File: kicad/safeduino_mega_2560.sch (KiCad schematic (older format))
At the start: 97 parts, among them X1 USBB-1J

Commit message: Продолжил переделывать SafeDuino MEGA 2560.
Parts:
- removed XP16, XP26, XP27, XP28, XP32, XP36, XP37, XP39, XP40, XP48, XP53, XP62, XP65, XP67, XP68, XP7: ~, IWconnectors:1_pin, symbol LFconnectors:PIN_M_1
- added LL1: MMZ2012R601AT000, IWsmd_case:SMD0805, symbol LFtransformator:INDUCTOR
- added XP7, XP8: PLS-2, IWconnectors:PIN_ARRAY_2x1, symbol LFconnectors:connector_2pin_gost
- added XS11: PBS-10, IWconnectors:PIN_ARRAY_10x1, symbol LFconnectors:connector_10pin_gost
- C13, C14, C15, C16, C17, C18, C19, C2, C20, C22, C23, C3, C4, C8, R10, R11, R12, R13, R14, R17, R18, R19, R2, R3, R4, R5, R6, R7, R8, R9: footprint IWsmd_case:SMD0805 -> IWsmd_case:SMD0603
- C6: value 100мк 10В -> 4.7 мк 50В
- DA1: value P10LU-0505ELF -> SPU03L-05
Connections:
- net labels added: USB_D+, USB_D-
- net labels removed: UD+, UD-
- wire segments 524 -> 523
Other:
- note added: "R19 необходим для создания импульса команды\nRESET на ATMEGA 2560 через конденсатор С2"
- note removed: "PB"
- note removed: "PD"
- note removed: "PE"
- note removed: "PH"
- note removed: "R19 необходим для подачи команды RESET на ATMEGA 2560 через\nконденсатор С2"
- moved on the sheet: C1, C6, DA1, FU1, VD8

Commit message: Продолжил переделывать печатную плату SafeDuino MEGA 2560.
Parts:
- XS10: value 2214SM-36G-75-PCP -> PBD-28; footprint IWconnectors:PIN_ARRAY_18x2 -> IWconnectors:PIN_ARRAY_14x2; symbol LFconnectors:connector_36pin_gost -> LFconnectors:connector_28pin_gost
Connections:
- wire segments 523 -> 515
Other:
- note removed: "PA0"
- note removed: "PA1"
- note removed: "PA2"
- note removed: "PA3"
- note removed: "PA4"
- note removed: "PA5"
- note removed: "PA6"
- note removed: "PA7"
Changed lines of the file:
@@
 Text Notes 19000 5050 0    60   ~ 0
 SCK
-Text Notes 19000 8150 0    60   ~ 0
-GND
 Text Notes 19000 6750 0    60   ~ 0
 PC2
 Text Notes 19000 6850 0    60   ~ 0
 PC3
-Text Notes 19000 7350 0    60   ~ 0
-PA7
-Text Notes 19000 7450 0    60   ~ 0
-PA6
-Text Notes 19000 7550 0    60   ~ 0
-PA5
-Text Notes 19000 7650 0    60   ~ 0
-PA4
-Text Notes 19000 7750 0    60   ~ 0
-PA3
-Text Notes 19000 7850 0    60   ~ 0
-PA2
-Text Notes 19000 7950 0    60   ~ 0
-PA1
-Text Notes 19000 8050 0    60   ~ 0
-PA0
-Text Notes 19000 8250 0    60   ~ 0
-GND
 Text Notes 19000 7250 0    60   ~ 0
 PC7
@@
 Text Notes 19000 7050 0    60   ~ 0
 PC5
-Connection ~ 18500 8200
+Connection ~ 18500 7400
 Text Label 18050 4700 0    60   ~ 0
 MPU_VCC
 Wire Wire Line
-	18500 8100 18500 8200
-Wire Wire Line
-	18600 8100 18500 8100
-Text Label 18050 8200 0    60   ~ 0
+	18500 7300 18500 7400
+Wire Wire Line
+	18600 7300 18500 7300
+Text Label 18050 7400 0    60   ~ 0
 GND
 Wire Wire Line
 	18600 4900 18050 4900
-Text Label 18050 4900 0    60   ~ 0
-PB0
 Wire Wire Line
 	18600 5000 18050 5000
-Text Label 18050 5000 0    60   ~ 0
-PB1
 Wire Wire Line
 	18600 5100 18050 5100
-Text Label 18050 5100 0    60   ~ 0
-PB2
 Wire Wire Line
 	18600 5200 18050 5200
-Text Label 18050 5200 0    60   ~ 0
-PB3
 Wire Wire Line
 	18600 5300 18050 5300
@@
 Text Label 18050 7200 0    60   ~ 0
 PC7
-Text Label 18050 7300 0    60   ~ 0
-PA7
-Text Label 18050 7400 0    60   ~ 0
-PA6
-Text Label 18050 7500 0    60   ~ 0
-PA5
-Text Label 18050 7600 0    60   ~ 0
-PA4
-Text Label 18050 7700 0    60   ~ 0
-PA3
-Text Label 18050 7800 0    60   ~ 0
-PA2
-Text Label 18050 7900 0    60   ~ 0
-PA1
-Text Label 18050 8000 0    60   ~ 0
-PA0
-Wire Wire Line
-	18600 8200 18500 8200
-$Comp
-L LFconnectors:connector_36pin_gost XS10
-U 1 1 64EB12AA
-P 18600 4700
-F 0 "XS10" H 18850 5050 71  0000 L CNN
-F 1 "2214SM-36G-75-PCP" H 18350 4950 71  0000 L CNN
-F 2 "IWconnectors:PIN_ARRAY_18x2" H 18950 4850 50  0001 C CNN
-F 3 "" H 18600 4700 60  0000 C CNN
-	1    18600 4700
-	1    0    0    -1
-$EndComp
+Wire Wire Line
+	18600 7400 18500 7400
 $Comp
 L LFtransformator:INDUCTOR LL1
@@
 	18050 7200 18600 7200
 Wire Wire Line
-	18050 7300 18600 7300
-Wire Wire Line
-	18050 7400 18600 7400
-Wire Wire Line
-	18050 7500 18600 7500
-Wire Wire Line
-	18050 7600 18600 7600
-Wire Wire Line
-	18050 7700 18600 7700
-Wire Wire Line
 	18050 6000 18600 6000
 Wire Wire Line
-	18050 7800 18600 7800
-Wire Wire Line
-	18050 7900 18600 7900
-Wire Wire Line
-	18050 8000 18600 8000
-Wire Wire Line
-	18050 8200 18500 8200
+	18050 7400 18500 7400
 Wire Wire Line
 	18050 6100 18600 6100
@@
 Text Notes 20400 9100 0    60   ~ 0
 GND
+Text Label 10350 3000 0    50   ~ 0
+PB0
+Text Label 10350 3100 0    50   ~ 0
+PB1
+Text Label 10350 3200 0    50   ~ 0
+PB2
+Text Label 10350 3300 0    50   ~ 0
+PB3
+Text Label 18050 5100 0    60   ~ 0
+MOSI
+Text Label 18050 5200 0    60   ~ 0
+MISO
+Text Label 18050 5000 0    60   ~ 0
+SCK
+Text Label 18050 4900 0    60   ~ 0
+SS
+Text Notes 19000 7350 0    60   ~ 0
+GND
+Text Notes 19000 7450 0    60   ~ 0
+GND
+$Comp
+L LFconnectors:connector_28pin_gost XS10
+U 1 1 64EB12AA
+P 18600 4700
+F 0 "XS10" H 18850 5050 71  0000 L CNN
+F 1 "PBD-28" H 18750 4950 71  0000 L CNN
+F 2 "IWconnectors:PIN_ARRAY_14x2" H 18950 4850 50  0001 C CNN
+F 3 "" H 18600 4700 60  0000 C CNN
+	1    18600 4700
+	1    0    0    -1
+$EndComp
 $EndSCHEMATC

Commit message: Закончил предварительную трассировку платы SafeDuino MEGA 2560.
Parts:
- XS11: value PBS-10 -> PBS-8; footprint IWconnectors:PIN_ARRAY_10x1 -> IWconnectors:PIN_ARRAY_8x1; symbol LFconnectors:connector_10pin_gost -> LFconnectors:connector_8pin_gost
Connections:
- wire segments 515 -> 513
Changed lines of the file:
@@
 Wire Wire Line
 	4800 8100 5250 8100
-Text Label 19600 8350 0    60   ~ 0
-SS
+Text Label 19600 8550 0    60   ~ 0
+PD4
+Text Label 19600 8650 0    60   ~ 0
+PD5
 Text Label 19600 8750 0    60   ~ 0
-PD4
+PD6
+Text Label 19600 8950 0    60   ~ 0
+PE7
+Text Label 19600 9050 0    60   ~ 0
+PE6
+Text Label 19600 9150 0    60   ~ 0
+PE2
+Text Label 19600 8450 0    60   ~ 0
+PH7
 Text Label 19600 8850 0    60   ~ 0
-PD5
-Text Label 19600 8950 0    60   ~ 0
-PD6
-Text Label 19600 8650 0    60   ~ 0
-PE7
-Text Label 19600 8550 0    60   ~ 0
-PE6
-Text Label 19600 8450 0    60   ~ 0
-PE2
-Text Label 19600 9150 0    60   ~ 0
-PH7
-Text Label 19600 9050 0    60   ~ 0
 PH2
-Wire Wire Line
-	19600 8350 20000 8350
 Wire Wire Line
 	19600 8750 20000 8750
@@
 Text Notes 18750 11500 0    60   ~ 0
 VCC
-$Comp
-L LFconnectors:connector_10pin_gost XS11
-U 1 1 643A5231
-P 20000 8350
-F 0 "XS11" H 20150 8700 71  0000 L CNN
-F 1 "PBS-10" H 20150 8600 71  0000 L CNN
-F 2 "IWconnectors:PIN_ARRAY_10x1" H 20350 8500 50  0001 C CNN
-F 3 "" H 20000 8350 60  0000 C CNN
-	1    20000 8350
-	1    0    0    -1
-$EndComp
-Text Label 19600 9250 0    60   ~ 0
-GND
-Wire Wire Line
-	19600 9250 20000 9250
 Text Notes 20400 9200 0    60   ~ 0
 GND
-Text Notes 20400 9300 0    60   ~ 0
-GND
 Wire Wire Line
 	18050 5900 18600 5900
@@
 Wire Wire Line
 	18050 6700 18600 6700
-Text Notes 20400 8400 0    60   ~ 0
-GND
 Text Notes 20400 8500 0    60   ~ 0
 GND
@@
 	1    0    0    -1
 $EndComp
+$Comp
+L LFconnectors:connector_8pin_gost XS11
+U 1 1 643A5231
+P 20000 8450
+F 0 "XS11" H 20150 8800 71  0000 L CNN
+F 1 "PBS-8" H 20150 8700 71  0000 L CNN
+F 2 "IWconnectors:PIN_ARRAY_8x1" H 20350 8600 50  0001 C CNN
+F 3 "" H 20000 8450 60  0000 C CNN
+	1    20000 8450
+	1    0    0    -1
+$EndComp

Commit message: Оптимизировал трассировку печатной платы.
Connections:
- net labels removed: PB0, PB1, PB2, PB3
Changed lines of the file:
@@
 L LFcomponents:QUARTZ_RESONATOR Z2
 U 1 1 5256C28E
-P 10500 8350
-F 0 "Z2" H 10650 8700 71  0000 C CNN
-F 1 "16МГц" H 10650 8600 71  0000 C CNN
-F 2 "IWcomponents:HC-49SM" H 10500 8350 60  0001 C CNN
-F 3 "" H 10500 8350 60  0001 C CNN
-	1    10500 8350
-	1    0    0    -1
+P 10800 8350
+F 0 "Z2" H 10950 8700 71  0000 C CNN
+F 1 "16МГц" H 10950 8600 71  0000 C CNN
+F 2 "IWcomponents:HC-49SM" H 10800 8350 60  0001 C CNN
+F 3 "" H 10800 8350 60  0001 C CNN
+	1    10800 8350
+	-1   0    0    -1
 $EndComp
 Text Label 10650 9050 1    60   ~ 0
@@
 Text Notes 20400 9100 0    60   ~ 0
 GND
-Text Label 10350 3000 0    50   ~ 0
-PB0
-Text Label 10350 3100 0    50   ~ 0
-PB1
-Text Label 10350 3200 0    50   ~ 0
-PB2
-Text Label 10350 3300 0    50   ~ 0
-PB3
 Text Label 18050 5100 0    60   ~ 0
 MOSI

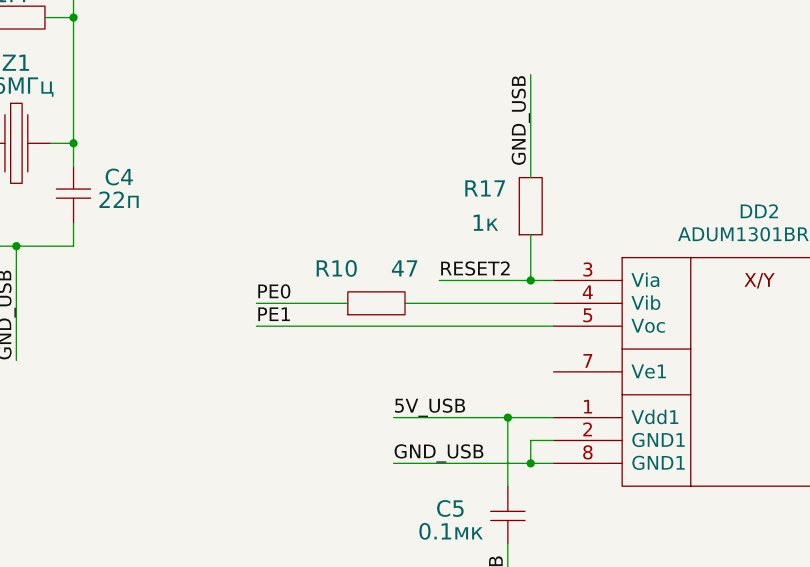
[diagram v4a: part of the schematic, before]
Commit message: Продолжил оптимизацию трассировки печатной платы.
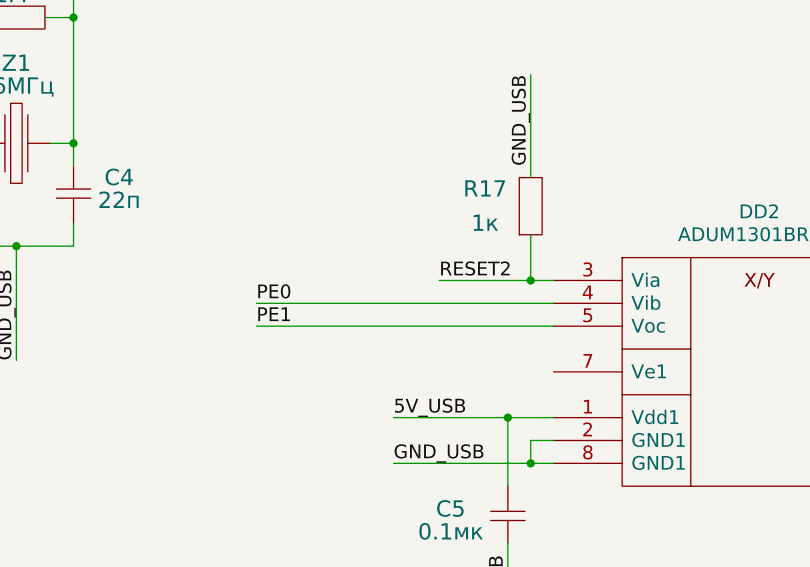
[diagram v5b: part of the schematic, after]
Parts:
- removed R10: 47, IWsmd_case:SMD0603, symbol LFresistor:RESISTOR
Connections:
- wire segments 513 -> 512
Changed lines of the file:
@@
 	7100 12800 7100 12900
 Wire Wire Line
-	6300 12200 5900 12200
-Wire Wire Line
 	5900 12300 7200 12300
-Wire Wire Line
-	7200 12200 6550 12200
 Wire Wire Line
 	20950 6400 21400 6400
@@
 Text Label 10500 12200 2    60   ~ 0
 RXD0
-$Comp
-L LFresistor:RESISTOR R10
-U 1 1 5260ED22
-P 6300 12200
-F 0 "R10" H 6250 12050 71  0000 C CNN
-F 1 "47" H 6550 12050 71  0000 C CNN
-F 2 "IWsmd_case:SMD0603" H 6300 12200 60  0001 C CNN
-F 3 "" H 6300 12200 60  0001 C CNN
-	1    6300 12200
-	1    0    0    1
-$EndComp
 Text Label 5900 12300 0    60   ~ 0
 PE1
@@
 	1    0    0    -1
 $EndComp
+Wire Wire Line
+	5900 12200 7200 12200
 $EndSCHEMATC

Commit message: Поправил схему для лучшей защиты от ЭМП и продолжил переделывать трассировку печатной платы.
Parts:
- removed C13, C14: 22п, IWsmd_case:SMD0603, symbol LFcapitors:CAPITORS
- removed R13, R7: 1M, IWsmd_case:SMD0603, symbol LFresistor:RESISTOR
- removed Z2: 16МГц, IWcomponents:HC-49SM, symbol LFcomponents:QUARTZ_RESONATOR
- added C24: 22мк 10В, IWsmd_case:CASE_B, symbol LFcapitors:CAPITORS_ELECTROLYTIC
- added C25: 0.1мк, IWsmd_case:SMD0603, symbol LFcapitors:CAPITORS
- added LL2: MMZ2012R601AT000, IWsmd_case:SMD0805, symbol LFtransformator:INDUCTOR
- added LL3: MMZ2012R600A, IWsmd_case:SMD0805, symbol LFtransformator:INDUCTOR
- added LL4: LQM21FN100N00L, IWsmd_case:SMD0805, symbol LFtransformator:INDUCTOR
- added Z2: CSTCE16M0V53-R0, IWsmd_case:CSTNE_G_8-13_99MHz, symbol LFcomponents:QUARTZ_CSTNE_G_CSTNE_V
- C1, C11, C12, C5, C9: footprint IWsmd_case:SMD0805 -> IWsmd_case:SMD0603
- C6: value 4.7 мк 50В -> 10 мк 25В
- C7: value 47мк 10В -> 22мк 10В
- LL1: value MMZ2012R601AT000 -> MMZ2012R600A
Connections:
- net labels added: RD+, RD-
- net labels removed: D+, D-
- wire segments 512 -> 507
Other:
- note added: "3.3V"
- note added: "ADC0"
- note added: "ADC1"
- note added: "ADC10"
- note added: "ADC11"
- note added: "ADC12"
- note added: "ADC13"
- note added: "ADC14"
- note added: "ADC15"
- note added: "ADC2"
- note added: "ADC3"
- note added: "ADC4"
- note added: "ADC5"
- note added: "ADC6"
- note added: "ADC7"
- note added: "ADC8"
- note added: "ADC9"
- note added: "PD4"
- note added: "PD5"
- note added: "PD6"
- note added: "PE2"
- note added: "PE6"
- note added: "PH2"
- note added: "PH7"
- note added: "VIN"
- moved on the sheet: C20, C21, C3, C4, C6, C7, DA1, DA3, R2, R3, VD1, VD2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

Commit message: Продолжил оптимизировать трассировку печатной платы.
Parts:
- removed C3, C4: 22п, IWsmd_case:SMD0603, symbol LFcapitors:CAPITORS
- removed R18: 1M, IWsmd_case:SMD0603, symbol LFresistor:RESISTOR
- removed VD7: PESD5V0L1BA,115, IWcomponents:SOD323, symbol LFdiod:STABILITRON_TWO
- removed Z1: 16МГц, IWcomponents:HC-49SM, symbol LFcomponents:QUARTZ_RESONATOR
- added Z1: CSTCE16M0V53-R0, IWsmd_case:CSTNE_G_8-13_99MHz, symbol LFcomponents:QUARTZ_CSTNE_G_CSTNE_V
- C24: value 22мк 10В -> 47мк 10В; footprint IWsmd_case:CASE_B -> IWsmd_case:CASE_C
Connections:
- wire segments 507 -> 492
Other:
- moved on the sheet: C1, C22, C23, R2, R3, R4, R6, VD3, VD4, VD8, Z3

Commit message: Продолжил оптимизировать трассировку печатной платы.
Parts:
- removed C12: 0.1мк, IWsmd_case:SMD0603, symbol LFcapitors:CAPITORS
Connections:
- wire segments 492 -> 488
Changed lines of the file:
@@
 	9650 10450 9650 10350
-Wire Wire Line
-	9200 10150 10650 10150
-Wire Wire Line
-	10650 10450 10650 10150
-Wire Wire Line
-	10650 10800 10650 10700
 Wire Wire Line
 	10150 10700 10150 10800
@@
 	9650 10700 9650 10800
 Connection ~ 10150 10250
-Connection ~ 10650 10150
 Connection ~ 9650 10350
 Wire Wire Line
@@
 Text Label 4600 12600 1    60   ~ 0
 GND_USB
-Text Label 11050 10150 2    60   ~ 0
+Text Label 10550 10150 2    60   ~ 0
 5V_USB
 Text Label 10550 10250 2    60   ~ 0
@@
 Text Label 10150 11300 1    60   ~ 0
 GND_USB
-$Comp
-L LFcapitors:CAPITORS C12
-U 1 1 52569AE0
-P 10650 10700
-F 0 "C12" V 10850 10450 71  0000 C CNN
-F 1 "0.1мк" V 10750 10450 71  0000 C CNN
-F 2 "IWsmd_case:SMD0603" H 10650 10700 60  0001 C CNN
-F 3 "" H 10650 10700 60  0001 C CNN
-	1    10650 10700
-	0    -1   -1   0
-$EndComp
 $Comp
 L LFcapitors:CAPITORS C11
@@
 	10150 10800 10150 11300
 Wire Wire Line
-	10150 10800 10650 10800
-Wire Wire Line
 	4700 5850 5250 5850
 Wire Wire Line
@@
 Wire Wire Line
 	10150 10250 10550 10250
-Wire Wire Line
-	10650 10150 11050 10150
 Wire Wire Line
 	9650 10350 10050 10350
@@
 	19600 9050 20000 9050
 Wire Wire Line
-	18500 4700 18600 4700
-Connection ~ 18500 4700
-Wire Wire Line
-	18500 4800 18500 4700
-Wire Wire Line
-	18600 4800 18500 4800
-Wire Wire Line
-	18050 4700 18500 4700
-Text Notes 19000 6150 0    60   ~ 0
+	18450 7400 18550 7400
+Connection ~ 18450 7400
+Wire Wire Line
+	18450 7300 18450 7400
+Wire Wire Line
+	18550 7300 18450 7300
+Wire Wire Line
+	18000 7400 18450 7400
+Text Notes 18950 6050 0    60   ~ 0
 PG0
-Text Notes 19000 6350 0    60   ~ 0
+Text Notes 18950 5850 0    60   ~ 0
 PG2
-Text Notes 19000 4750 0    60   ~ 0
-+5V
-Text Notes 19000 4850 0    60   ~ 0
-+5V
-Text Notes 19000 5350 0    60   ~ 0
+Text Notes 18950 7450 0    60   ~ 0
+GND
+Text Notes 18950 7350 0    60   ~ 0
+GND
+Text Notes 18950 6850 0    60   ~ 0
 PL0
-Text Notes 19000 5450 0    60   ~ 0
+Text Notes 18950 6750 0    60   ~ 0
 PL1
-Text Notes 19000 5550 0    60   ~ 0
+Text Notes 18950 6650 0    60   ~ 0
 PL2
-Text Notes 19000 5650 0    60   ~ 0
+Text Notes 18950 6550 0    60   ~ 0
 PL3
-Text Notes 19000 5750 0    60   ~ 0
+Text Notes 18950 6450 0    60   ~ 0
 PL4
-Text Notes 19000 5850 0    60   ~ 0
+Text Notes 18950 6350 0    60   ~ 0
 PL5
-Text Notes 19000 5950 0    60   ~ 0
+Text Notes 18950 6250 0    60   ~ 0
 PL6
-Text Notes 19000 6050 0    60   ~ 0
+Text Notes 18950 6150 0    60   ~ 0
 PL7
-Text Notes 19000 6250 0    60   ~ 0
+Text Notes 18950 5950 0    60   ~ 0
 PG1
-Text Notes 19000 6450 0    60   ~ 0
+Text Notes 18950 5750 0    60   ~ 0
 PD7
-Text Notes 19000 6550 0    60   ~ 0
+Text Notes 18950 5650 0    60   ~ 0
 PC0
-Text Notes 19000 6650 0    60   ~ 0
+Text Notes 18950 5550 0    60   ~ 0
 PC1
-Text Notes 19000 5250 0    60   ~ 0
+Text Notes 18950 6950 0    60   ~ 0
 MISO
-Text Notes 19000 5150 0    60   ~ 0
+Text Notes 18950 7050 0    60   ~ 0
 MOSI
-Text Notes 19000 4950 0    60   ~ 0
+Text Notes 18950 7250 0    60   ~ 0
 SS
-Text Notes 19000 5050 0    60   ~ 0
+Text Notes 18950 7150 0    60   ~ 0
 SCK
-Text Notes 19000 6750 0    60   ~ 0
+Text Notes 18950 5450 0    60   ~ 0
 PC2
-Text Notes 19000 6850 0    60   ~ 0
+Text Notes 18950 5350 0    60   ~ 0
 PC3
-Text Notes 19000 7250 0    60   ~ 0
+Text Notes 18950 4950 0    60   ~ 0
 PC7
-Text Notes 19000 7150 0    60   ~ 0
+Text Notes 18950 5050 0    60   ~ 0
 PC6
-Text Notes 19000 6950 0    60   ~ 0
+Text Notes 18950 5250 0    60   ~ 0
 PC4
-Text Notes 19000 7050 0    60   ~ 0
+Text Notes 18950 5150 0    60   ~ 0
 PC5
-Connection ~ 18500 7400
-Text Label 18050 4700 0    60   ~ 0
+Connection ~ 18450 4700
+Text Label 18000 4700 0    60   ~ 0
 MPU_VCC
 Wire Wire Line
-	18500 7300 18500 7400
-Wire Wire Line
-	18600 7300 18500 7300
-Text Label 18050 7400 0    60   ~ 0
-GND
-Wire Wire Line
-	18600 4900 18050 4900
-Wire Wire Line
-	18600 5000 18050 5000
-Wire Wire Line
-	18600 5100 18050 5100
-Wire Wire Line
-	18600 5200 18050 5200
-Wire Wire Line
-	18600 5300 18050 5300
-Text Label 18050 5300 0    60   ~ 0
+	18450 4800 18450 4700
+Wire Wire Line
+	18550 4800 18450 4800
+Text Label 18000 7400 0    60   ~ 0
+GND
+Wire Wire Line
+	18550 7200 18000 7200
+Wire Wire Line
+	18550 7100 18000 7100
+Wire Wire Line
+	18550 7000 18000 7000
+Wire Wire Line
+	18550 6900 18000 6900
+Wire Wire Line
+	18550 6800 18000 6800
+Text Label 18000 6800 0    60   ~ 0
 PL0
 Wire Wire Line
-	18600 5400 18050 5400
-Text Label 18050 5400 0    60   ~ 0
+	18550 6700 18000 6700
+Text Label 18000 6700 0    60   ~ 0
 PL1
 Wire Wire Line
-	18600 5500 18050 5500
-Text Label 18050 5500 0    60   ~ 0
+	18550 6600 18000 6600
+Text Label 18000 6600 0    60   ~ 0
 PL2
 Wire Wire Line
-	18600 5600 18050 5600
-Text Label 18050 5600 0    60   ~ 0
+	18550 6500 18000 6500
+Text Label 18000 6500 0    60   ~ 0
 PL3
 Wire Wire Line
-	18600 5700 18050 5700
-Text Label 18050 5700 0    60   ~ 0
+	18550 6400 18000 6400
+Text Label 18000 6400 0    60   ~ 0
 PL4
 Wire Wire Line
-	18600 5800 18050 5800
-Text Label 18050 5800 0    60   ~ 0
+	18550 6300 18000 6300
+Text Label 18000 6300 0    60   ~ 0
 PL5
-Text Label 18050 5900 0    60   ~ 0
+Text Label 18000 6200 0    60   ~ 0
 PL6
-Text Label 18050 6000 0    60   ~ 0
+Text Label 18000 6100 0    60   ~ 0
 PL7
-Text Label 18050 6100 0    60   ~ 0
+Text Label 18000 6000 0    60   ~ 0
 PG0
-Text Label 18050 6200 0    60   ~ 0
+Text Label 18000 5900 0    60   ~ 0
 PG1
-Text Label 18050 6300 0    60   ~ 0
+Text Label 18000 5800 0    60   ~ 0
 PG2
-Text Label 18050 6400 0    60   ~ 0
+Text Label 18000 5700 0    60   ~ 0
 PD7
-Text Label 18050 6500 0    60   ~ 0
+Text Label 18000 5600 0    60   ~ 0
 PC0
-Text Label 18050 6600 0    60   ~ 0
+Text Label 18000 5500 0    60   ~ 0
 PC1
-Text Label 18050 6700 0    60   ~ 0
+Text Label 18000 5400 0    60   ~ 0
 PC2
-Text Label 18050 6800 0    60   ~ 0
+Text Label 18000 5300 0    60   ~ 0
 PC3
-Text Label 18050 6900 0    60   ~ 0
+Text Label 18000 5200 0    60   ~ 0
 PC4
-Text Label 18050 7000 0    60   ~ 0
+Text Label 18000 5100 0    60   ~ 0
 PC5
-Text Label 18050 7100 0    60   ~ 0
+Text Label 18000 5000 0    60   ~ 0
 PC6
-Text Label 18050 7200 0    60   ~ 0
+Text Label 18000 4900 0    60   ~ 0
 PC7
 Wire Wire Line
-	18600 7400 18500 7400
+	18550 4700 18450 4700
 $Comp
 L LFtransformator:INDUCTOR LL1
@@
 PE2
 Wire Wire Line
-	18050 5900 18600 5900
-Wire Wire Line
-	18050 6800 18600 6800
-Wire Wire Line
-	18050 6900 18600 6900
-Wire Wire Line
-	18050 7000 18600 7000
-Wire Wire Line
-	18050 7100 18600 7100
-Wire Wire Line
-	18050 7200 18600 7200
-Wire Wire Line
-	18050 6000 18600 6000
-Wire Wire Line
-	18050 7400 18500 7400
-Wire Wire Line
-	18050 6100 18600 6100
-Wire Wire Line
-	18050 6200 18600 6200
-Wire Wire Line
-	18050 6300 18600 6300
-Wire Wire Line
-	18050 6400 18600 6400
-Wire Wire Line
-	18050 6500 18600 6500
-Wire Wire Line
-	18050 6600 18600 6600
-Wire Wire Line
-	18050 6700 18600 6700
+	18000 6200 18550 6200
+Wire Wire Line
+	18000 5300 18550 5300
+Wire Wire Line
+	18000 5200 18550 5200
+Wire Wire Line
+	18000 5100 18550 5100
+Wire Wire Line
+	18000 5000 18550 5000
+Wire Wire Line
+	18000 4900 18550 4900
+Wire Wire Line
+	18000 6100 18550 6100
+Wire Wire Line
+	18000 4700 18450 4700
+Wire Wire Line
+	18000 6000 18550 6000
+Wire Wire Line
+	18000 5900 18550 5900
+Wire Wire Line
+	18000 5800 18550 5800
+Wire Wire Line
+	18000 5700 18550 5700
+Wire Wire Line
+	18000 5600 18550 5600
+Wire Wire Line
+	18000 5500 18550 5500
+Wire Wire Line
+	18000 5400 18550 5400
 Text Notes 20400 8500 0    60   ~ 0
 PH7
@@
 Text Notes 20400 9100 0    60   ~ 0
 PE6
-Text Label 18050 5100 0    60   ~ 0
+Text Label 18000 7000 0    60   ~ 0
 MOSI
-Text Label 18050 5200 0    60   ~ 0
+Text Label 18000 6900 0    60   ~ 0
 MISO
-Text Label 18050 5000 0    60   ~ 0
+Text Label 18000 7100 0    60   ~ 0
 SCK
-Text Label 18050 4900 0    60   ~ 0
+Text Label 18000 7200 0    60   ~ 0
 SS
-Text Notes 19000 7350 0    60   ~ 0
-GND
-Text Notes 19000 7450 0    60   ~ 0
-GND
+Text Notes 18950 4850 0    60   ~ 0
++5V
+Text Notes 18950 4750 0    60   ~ 0
++5V
 $Comp
 L LFconnectors:connector_28pin_gost XS10
 U 1 1 64EB12AA
-P 18600 4700
-F 0 "XS10" H 18850 5050 71  0000 L CNN
-F 1 "PBD-28" H 18750 4950 71  0000 L CNN
-F 2 "IWconnectors:PIN_ARRAY_14x2" H 18950 4850 50  0001 C CNN
-F 3 "" H 18600 4700 60  0000 C CNN
-	1    18600 4700
+P 18550 4700
+F 0 "XS10" H 18800 5050 71  0000 L CNN
+F 1 "PBD-28" H 18700 4950 71  0000 L CNN
+F 2 "IWconnectors:PIN_ARRAY_14x2" H 18900 4850 50  0001 C CNN
+F 3 "" H 18550 4700 60  0000 C CNN
+	1    18550 4700
 	1    0    0    -1
 $EndComp
@@
 Wire Wire Line
 	4050 11450 4150 11450
+Wire Wire Line
+	9200 10150 10550 10150
 $EndSCHEMATC
